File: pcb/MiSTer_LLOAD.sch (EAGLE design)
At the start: 22 parts, among them K1 692121030100

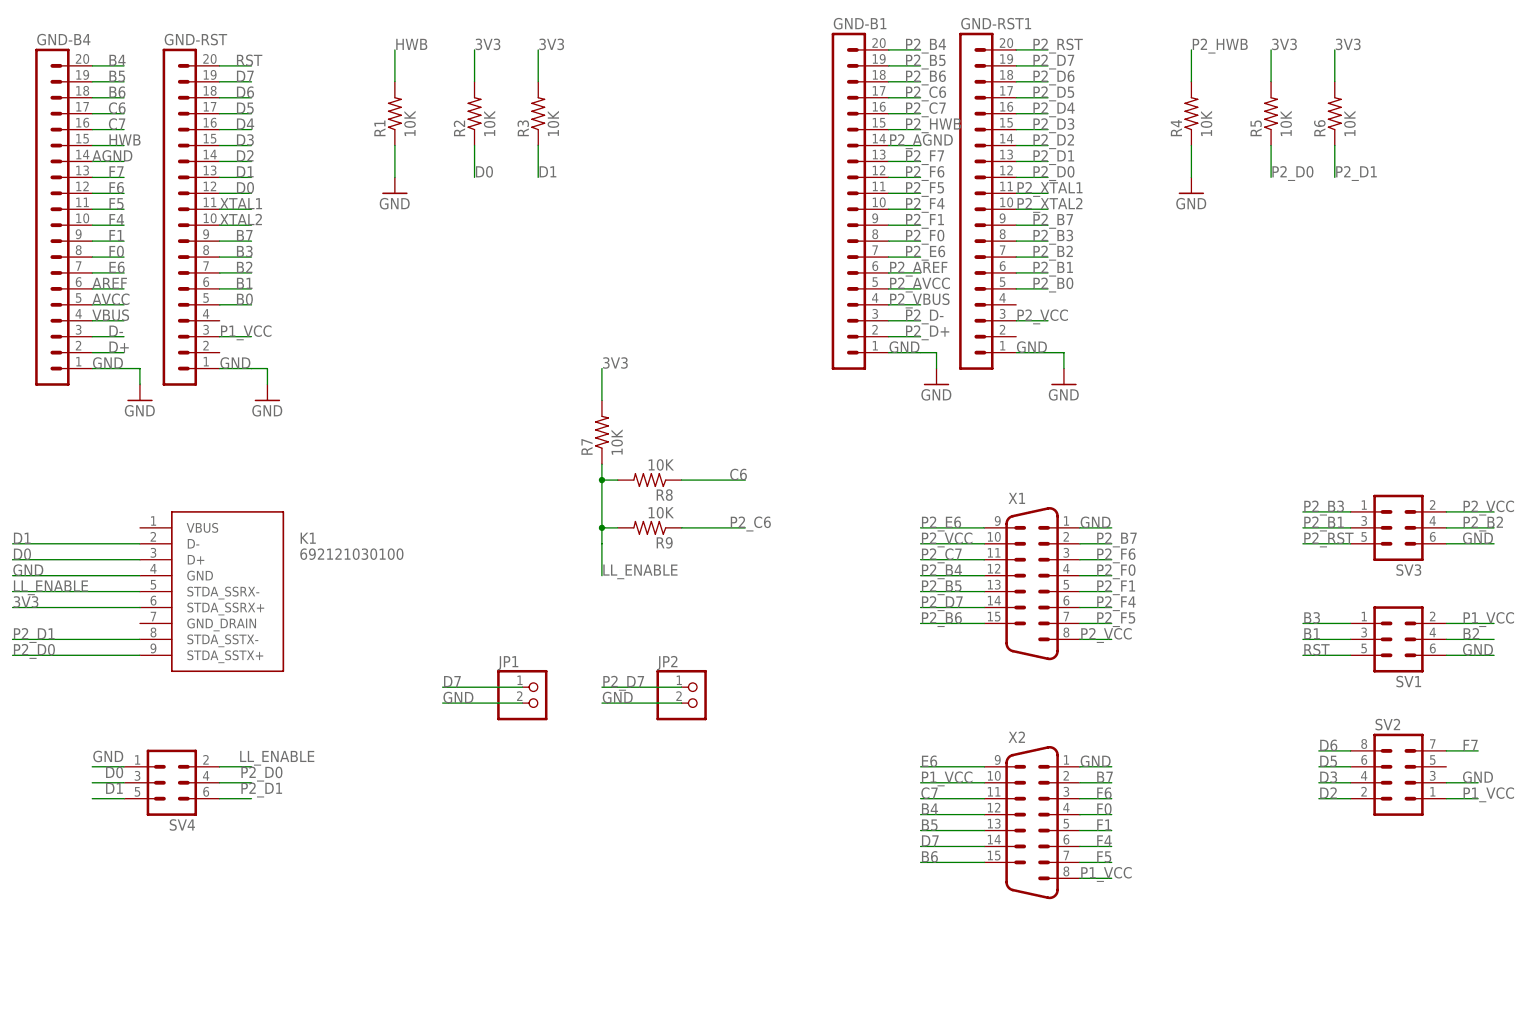
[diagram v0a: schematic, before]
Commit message: Proto v0.3 PCB - It does not rely on Serial IO VCC anymore
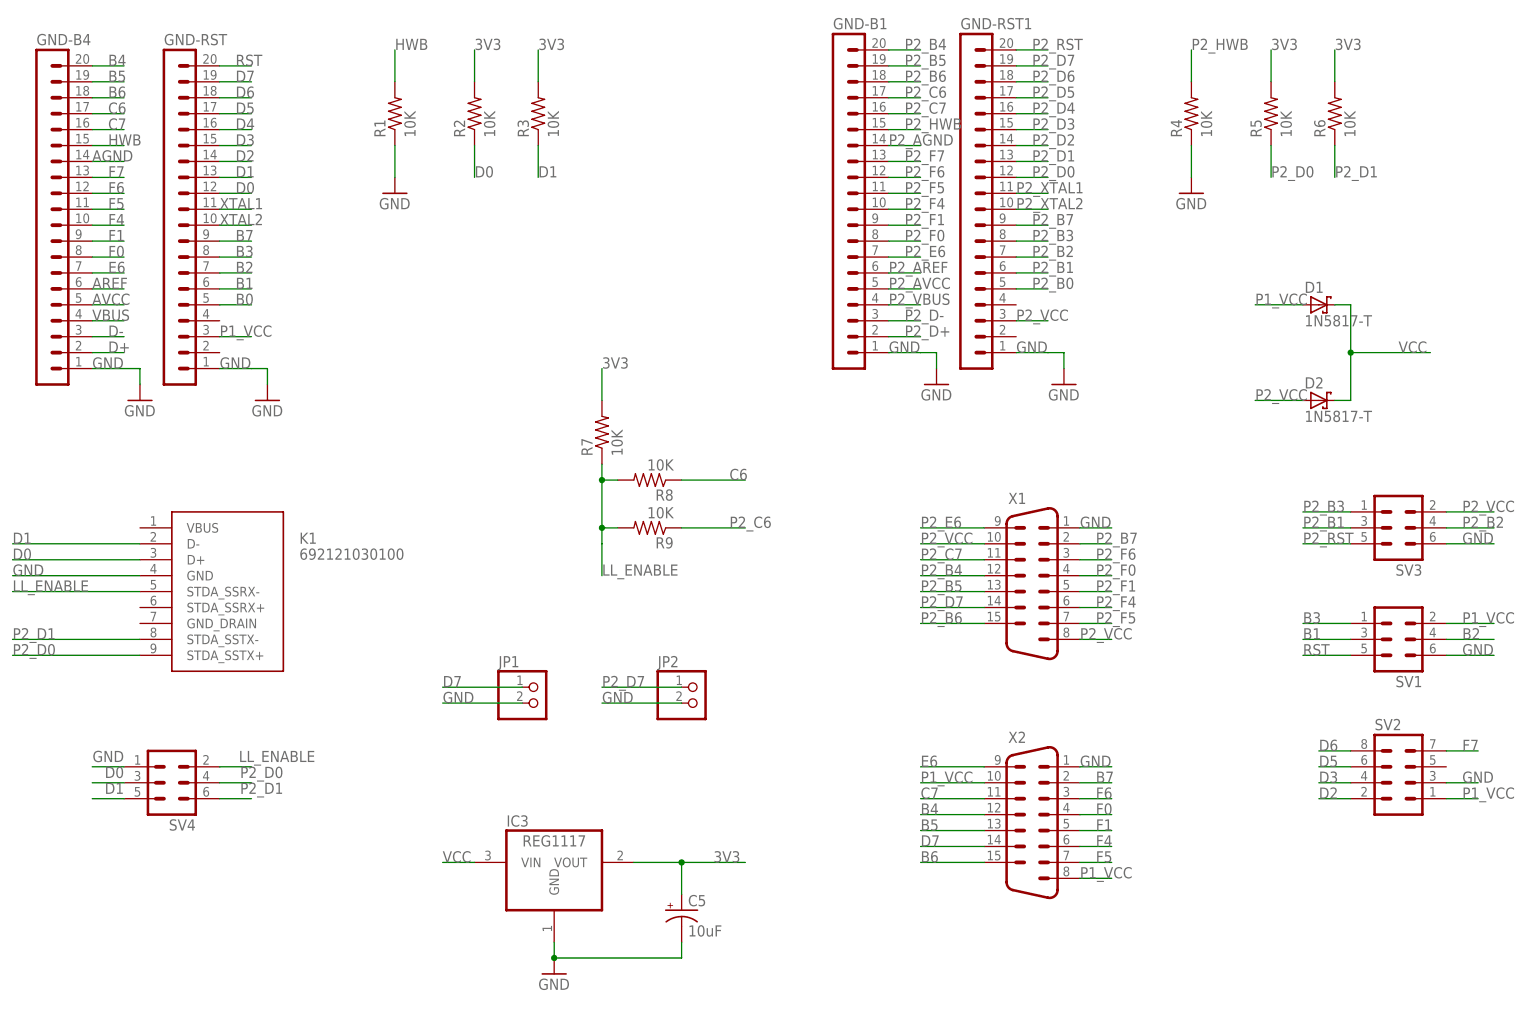
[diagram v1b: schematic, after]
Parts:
- added C5: 10uF, rcl:CPOL-USE2.5-6
- added D1, D2: 1N5817-T, diode:1N5817-T
- added IC3: REG1117, burr-brown:REG1117
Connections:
- new net VCC: D1.C, D2.C, IC3.VIN
- net 3V3: now also C5.+, IC3.VOUT; no longer K1.STDA_SSRX+
- net GND: now also C5.-, IC3.GND
- net P1_VCC: now also D1.A
- net P2_VCC: now also D2.A
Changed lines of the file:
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@@
 <part name="JP1" library="pinhead" deviceset="PINHD-1X2" device=""/>
 <part name="JP2" library="pinhead" deviceset="PINHD-1X2" device=""/>
+<part name="IC3" library="burr-brown" deviceset="REG1117" device=""/>
+<part name="GND7" library="supply1" deviceset="GND" device=""/>
+<part name="C5" library="rcl" deviceset="CPOL-US" device="E2.5-6" value="10uF"/>
+<part name="D1" library="diode" deviceset="1N581*" device="" technology="7-T"/>
+<part name="D2" library="diode" deviceset="1N581*" device="" technology="7-T"/>
 </parts>
 <sheets>
@@
 <instance part="JP1" gate="G$1" x="-35.56" y="-99.06"/>
 <instance part="JP2" gate="G$1" x="-10.16" y="-99.06"/>
+<instance part="IC3" gate="G$1" x="-33.02" y="-124.46"/>
+<instance part="GND7" gate="1" x="-33.02" y="-142.24"/>
+<instance part="C5" gate="G$1" x="-12.7" y="-132.08"/>
+<instance part="D1" gate="G$1" x="88.9" y="-35.56"/>
+<instance part="D2" gate="G$1" x="88.9" y="-50.8"/>
 </instances>
 <busses>
@@
 <label x="-25.4" y="-99.06" size="1.778" layer="95"/>
 </segment>
+<segment>
+<pinref part="IC3" gate="G$1" pin="GND"/>
+<pinref part="GND7" gate="1" pin="GND"/>
+<wire x1="-33.02" y1="-137.16" x2="-33.02" y2="-139.7" width="0.1524" layer="91"/>
+<pinref part="C5" gate="G$1" pin="-"/>
+<wire x1="-33.02" y1="-139.7" x2="-12.7" y2="-139.7" width="0.1524" layer="91"/>
+<wire x1="-12.7" y1="-139.7" x2="-12.7" y2="-137.16" width="0.1524" layer="91"/>
+<junction x="-33.02" y="-139.7"/>
+</segment>
 </net>
 <net name="RST" class="0">
@@
 <net name="3V3" class="0">
 <segment>
-<pinref part="K1" gate="G$1" pin="STDA_SSRX+"/>
-<wire x1="-99.06" y1="-83.82" x2="-119.38" y2="-83.82" width="0.1524" layer="91"/>
-<label x="-119.38" y="-83.82" size="1.778" layer="95"/>
-</segment>
-<segment>
 <pinref part="R2" gate="G$1" pin="2"/>
 <wire x1="-45.72" y1="0" x2="-45.72" y2="5.08" width="0.1524" layer="91"/>
@@
 <wire x1="-25.4" y1="-50.8" x2="-25.4" y2="-45.72" width="0.1524" layer="91"/>
 <label x="-25.4" y="-45.72" size="1.778" layer="95"/>
+</segment>
+<segment>
+<pinref part="IC3" gate="G$1" pin="VOUT"/>
+<wire x1="-20.32" y1="-124.46" x2="-12.7" y2="-124.46" width="0.1524" layer="91"/>
+<pinref part="C5" gate="G$1" pin="+"/>
+<wire x1="-12.7" y1="-124.46" x2="-2.54" y2="-124.46" width="0.1524" layer="91"/>
+<wire x1="-12.7" y1="-129.54" x2="-12.7" y2="-124.46" width="0.1524" layer="91"/>
+<junction x="-12.7" y="-124.46"/>
+<label x="-7.62" y="-124.46" size="1.778" layer="95"/>
 </segment>
 </net>
@@
 <pinref part="SV2" gate="G$1" pin="1"/>
 </segment>
+<segment>
+<wire x1="86.36" y1="-35.56" x2="78.74" y2="-35.56" width="0.1524" layer="91"/>
+<label x="78.74" y="-35.56" size="1.778" layer="95"/>
+<pinref part="D1" gate="G$1" pin="A"/>
+</segment>
 </net>
 <net name="P2_VCC" class="0">
@@
 <label x="111.76" y="-68.58" size="1.778" layer="95"/>
 </segment>
-</net>
+<segment>
+<wire x1="86.36" y1="-50.8" x2="78.74" y2="-50.8" width="0.1524" layer="91"/>
+<label x="78.74" y="-50.8" size="1.778" layer="95"/>
+<pinref part="D2" gate="G$1" pin="A"/>
+</segment>
+</net>
+<net name="VCC" class="0">
+<segment>
+<pinref part="IC3" gate="G$1" pin="VIN"/>
+<wire x1="-45.72" y1="-124.46" x2="-50.8" y2="-124.46" width="0.1524" layer="91"/>
+<label x="-50.8" y="-124.46" size="1.778" layer="95"/>
+</segment>
+<segment>
+<wire x1="93.98" y1="-43.18" x2="106.68" y2="-43.18" width="0.1524" layer="91"/>
+<wire x1="91.44" y1="-35.56" x2="93.98" y2="-35.56" width="0.1524" layer="91"/>
+<wire x1="93.98" y1="-35.56" x2="93.98" y2="-43.18" width="0.1524" layer="91"/>
+<wire x1="91.44" y1="-50.8" x2="93.98" y2="-50.8" width="0.1524" layer="91"/>
+<wire x1="93.98" y1="-50.8" x2="93.98" y2="-43.18" width="0.1524" layer="91"/>
+<junction x="93.98" y="-43.18"/>
+<label x="101.6" y="-43.18" size="1.778" layer="95"/>
+<pinref part="D1" gate="G$1" pin="C"/>
+<pinref part="D2" gate="G$1" pin="C"/>
+</segment>
+</net>

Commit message: Promoting LLOAD PCB to v1.0
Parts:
- removed SV2: (no value), con-lstb:MA04-2
- removed SV4: (no value), con-lstb:MA03-2
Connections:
- net 3V3: now also X1.10, X2.10
- net D0: no longer SV4.3
- net D1: no longer SV4.5
- net D2: no longer SV2.2
- net D3: no longer SV2.4
- net D5: no longer SV2.6
- net D6: no longer SV2.8
- net F7: no longer SV2.7
- net GND: no longer SV2.3, SV4.1
- net LL_ENABLE: no longer SV4.2
- net P1_VCC: no longer SV2.1, X2.10
- net P2_D0: no longer SV4.4
- net P2_D1: no longer SV4.6
- net P2_VCC: no longer X1.10
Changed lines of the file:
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@@
 <part name="FRAME1" library="frames" deviceset="A4L-LOC" device=""/>
 <part name="X2" library="con-subd" deviceset="M15" device="HP"/>
-<part name="SV2" library="con-lstb" deviceset="MA04-2" device=""/>
 <part name="R1" library="rcl" deviceset="R-US_" device="0207/10" value="10K"/>
 <part name="GND3" library="supply1" deviceset="GND" device=""/>
@@
 <part name="R8" library="rcl" deviceset="R-US_" device="0207/10" value="10K"/>
 <part name="R9" library="rcl" deviceset="R-US_" device="0207/10" value="10K"/>
-<part name="SV4" library="con-lstb" deviceset="MA03-2" device=""/>
 <part name="JP1" library="pinhead" deviceset="PINHD-1X2" device=""/>
 <part name="JP2" library="pinhead" deviceset="PINHD-1X2" device=""/>
@@
 <instance part="FRAME1" gate="G$1" x="-132.08" y="-162.56"/>
 <instance part="X2" gate="-1" x="43.18" y="-116.84"/>
-<instance part="SV2" gate="G$1" x="101.6" y="-109.22"/>
 <instance part="R1" gate="G$1" x="-58.42" y="-5.08" rot="R90"/>
 <instance part="GND3" gate="1" x="-58.42" y="-17.78"/>
@@
 <instance part="R8" gate="G$1" x="-17.78" y="-63.5" rot="R180"/>
 <instance part="R9" gate="G$1" x="-17.78" y="-71.12" rot="R180"/>
-<instance part="SV4" gate="1" x="-93.98" y="-111.76" rot="R180"/>
 <instance part="JP1" gate="G$1" x="-35.56" y="-99.06"/>
 <instance part="JP2" gate="G$1" x="-10.16" y="-99.06"/>
@@
 <pinref part="GND-B4" gate="1" pin="13"/>
 </segment>
-<segment>
-<wire x1="109.22" y1="-106.68" x2="114.3" y2="-106.68" width="0.1524" layer="91"/>
-<label x="111.76" y="-106.68" size="1.778" layer="95"/>
-<pinref part="SV2" gate="G$1" pin="7"/>
-</segment>
 </net>
 <net name="F6" class="0">
@@
 </segment>
 <segment>
-<wire x1="109.22" y1="-111.76" x2="114.3" y2="-111.76" width="0.1524" layer="91"/>
-<label x="111.76" y="-111.76" size="1.778" layer="95"/>
-<pinref part="SV2" gate="G$1" pin="3"/>
-</segment>
-<segment>
 <pinref part="R1" gate="G$1" pin="1"/>
 <pinref part="GND3" gate="1" pin="GND"/>
@@
 <wire x1="109.22" y1="-73.66" x2="116.84" y2="-73.66" width="0.1524" layer="91"/>
 <label x="111.76" y="-73.66" size="1.778" layer="95"/>
-</segment>
-<segment>
-<pinref part="SV4" gate="1" pin="1"/>
-<wire x1="-101.6" y1="-109.22" x2="-106.68" y2="-109.22" width="0.1524" layer="91"/>
-<label x="-101.6" y="-106.68" size="1.778" layer="95" rot="R180"/>
 </segment>
 <segment>
@@
 <pinref part="GND-RST" gate="1" pin="18"/>
 </segment>
-<segment>
-<wire x1="93.98" y1="-106.68" x2="88.9" y2="-106.68" width="0.1524" layer="91"/>
-<label x="88.9" y="-106.68" size="1.778" layer="95"/>
-<pinref part="SV2" gate="G$1" pin="8"/>
-</segment>
 </net>
 <net name="D5" class="0">
@@
 <pinref part="GND-RST" gate="1" pin="17"/>
 </segment>
-<segment>
-<wire x1="93.98" y1="-109.22" x2="88.9" y2="-109.22" width="0.1524" layer="91"/>
-<label x="88.9" y="-109.22" size="1.778" layer="95"/>
-<pinref part="SV2" gate="G$1" pin="6"/>
-</segment>
 </net>
 <net name="D4" class="0">
@@
 <pinref part="GND-RST" gate="1" pin="15"/>
 </segment>
-<segment>
-<wire x1="93.98" y1="-111.76" x2="88.9" y2="-111.76" width="0.1524" layer="91"/>
-<label x="88.9" y="-111.76" size="1.778" layer="95"/>
-<pinref part="SV2" gate="G$1" pin="4"/>
-</segment>
 </net>
 <net name="D2" class="0">
@@
 <pinref part="GND-RST" gate="1" pin="14"/>
 </segment>
-<segment>
-<wire x1="93.98" y1="-114.3" x2="88.9" y2="-114.3" width="0.1524" layer="91"/>
-<label x="88.9" y="-114.3" size="1.778" layer="95"/>
-<pinref part="SV2" gate="G$1" pin="2"/>
-</segment>
 </net>
 <net name="D1" class="0">
@@
 <label x="-35.56" y="-15.24" size="1.778" layer="95"/>
 </segment>
-<segment>
-<pinref part="SV4" gate="1" pin="5"/>
-<wire x1="-101.6" y1="-114.3" x2="-106.68" y2="-114.3" width="0.1524" layer="91"/>
-<label x="-101.6" y="-111.76" size="1.778" layer="95" rot="R180"/>
-</segment>
 </net>
 <net name="D0" class="0">
@@
 <label x="-45.72" y="-15.24" size="1.778" layer="95"/>
 </segment>
-<segment>
-<pinref part="SV4" gate="1" pin="3"/>
-<wire x1="-101.6" y1="-111.76" x2="-106.68" y2="-111.76" width="0.1524" layer="91"/>
-<label x="-101.6" y="-109.22" size="1.778" layer="95" rot="R180"/>
-</segment>
 </net>
 <net name="XTAL1" class="0">
@@
 <label x="91.44" y="-15.24" size="1.778" layer="95"/>
 </segment>
-<segment>
-<pinref part="SV4" gate="1" pin="6"/>
-<wire x1="-86.36" y1="-114.3" x2="-81.28" y2="-114.3" width="0.1524" layer="91"/>
-<label x="-76.2" y="-111.76" size="1.778" layer="95" rot="R180"/>
-</segment>
 </net>
 <net name="P2_D0" class="0">
@@
 <wire x1="81.28" y1="-10.16" x2="81.28" y2="-15.24" width="0.1524" layer="91"/>
 <label x="81.28" y="-15.24" size="1.778" layer="95"/>
-</segment>
-<segment>
-<pinref part="SV4" gate="1" pin="4"/>
-<wire x1="-86.36" y1="-111.76" x2="-81.28" y2="-111.76" width="0.1524" layer="91"/>
-<label x="-76.2" y="-109.22" size="1.778" layer="95" rot="R180"/>
 </segment>
 </net>
@@
 <junction x="-12.7" y="-124.46"/>
 <label x="-7.62" y="-124.46" size="1.778" layer="95"/>
+</segment>
+<segment>
+<wire x1="35.56" y1="-73.66" x2="25.4" y2="-73.66" width="0.1524" layer="91"/>
+<label x="25.4" y="-73.66" size="1.778" layer="95"/>
+<pinref part="X1" gate="-1" pin="10"/>
+</segment>
+<segment>
+<wire x1="35.56" y1="-111.76" x2="25.4" y2="-111.76" width="0.1524" layer="91"/>
+<label x="25.4" y="-111.76" size="1.778" layer="95"/>
+<pinref part="X2" gate="-1" pin="10"/>
 </segment>
 </net>
@@
 <wire x1="-25.4" y1="-73.66" x2="-25.4" y2="-78.74" width="0.1524" layer="91"/>
 </segment>
-<segment>
-<pinref part="SV4" gate="1" pin="2"/>
-<wire x1="-86.36" y1="-109.22" x2="-81.28" y2="-109.22" width="0.1524" layer="91"/>
-<label x="-71.12" y="-106.68" size="1.778" layer="95" rot="R180"/>
-</segment>
 </net>
 <net name="P1_VCC" class="0">
@@
 </segment>
 <segment>
-<wire x1="35.56" y1="-111.76" x2="25.4" y2="-111.76" width="0.1524" layer="91"/>
-<label x="25.4" y="-111.76" size="1.778" layer="95"/>
-<pinref part="X2" gate="-1" pin="10"/>
-</segment>
-<segment>
 <wire x1="50.8" y1="-127" x2="55.88" y2="-127" width="0.1524" layer="91"/>
 <label x="50.8" y="-127" size="1.778" layer="95"/>
@@
 </segment>
 <segment>
-<wire x1="109.22" y1="-114.3" x2="114.3" y2="-114.3" width="0.1524" layer="91"/>
-<label x="111.76" y="-114.3" size="1.778" layer="95"/>
-<pinref part="SV2" gate="G$1" pin="1"/>
-</segment>
-<segment>
 <wire x1="86.36" y1="-35.56" x2="78.74" y2="-35.56" width="0.1524" layer="91"/>
 <label x="78.74" y="-35.56" size="1.778" layer="95"/>
@@
 </segment>
 <segment>
-<wire x1="35.56" y1="-73.66" x2="25.4" y2="-73.66" width="0.1524" layer="91"/>
-<label x="25.4" y="-73.66" size="1.778" layer="95"/>
-<pinref part="X1" gate="-1" pin="10"/>
-</segment>
-<segment>

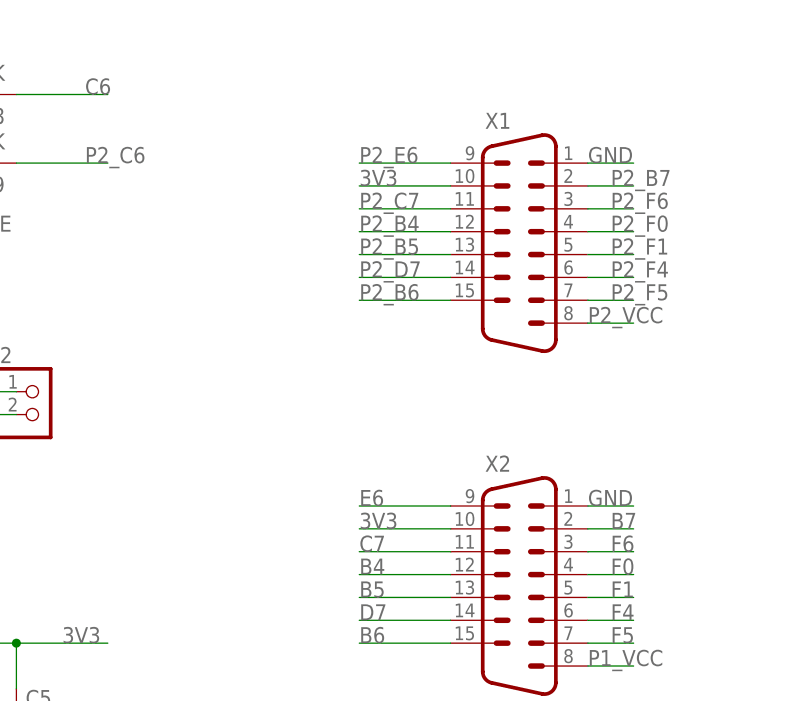
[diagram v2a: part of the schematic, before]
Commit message: Removed alternate VCC (3.3v) from DB15 pin 10. This will not make it directly compatible with supergun input, but at least no harm will be done in case someone inadvertently uses a supergun with it. Neo Geo and Neo Geo CD are still welcome in both revisions.
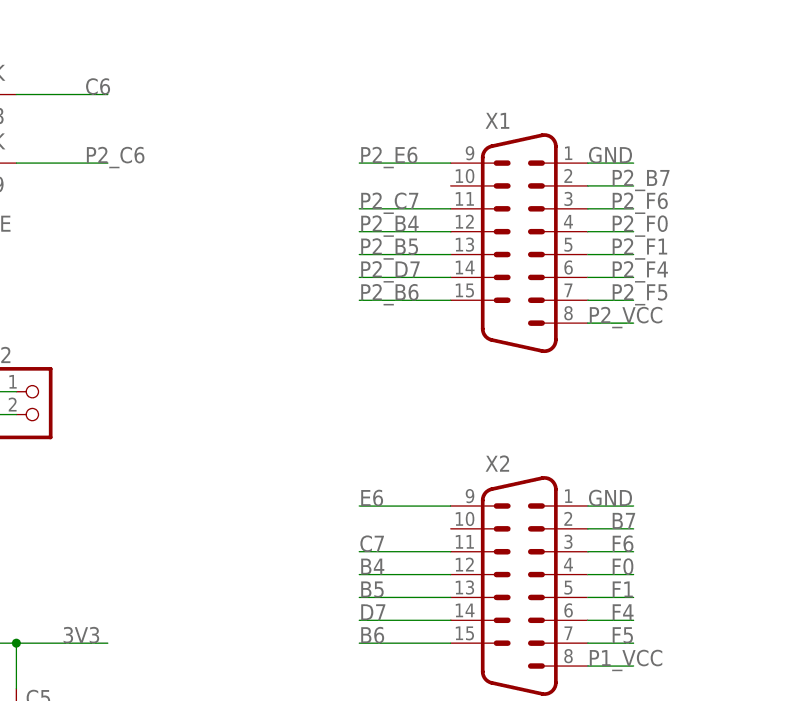
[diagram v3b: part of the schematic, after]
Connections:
- net 3V3: no longer X1.10, X2.10
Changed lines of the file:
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@@
 <label x="-7.62" y="-124.46" size="1.778" layer="95"/>
-</segment>
-<segment>
-<wire x1="35.56" y1="-73.66" x2="25.4" y2="-73.66" width="0.1524" layer="91"/>
-<label x="25.4" y="-73.66" size="1.778" layer="95"/>
-<pinref part="X1" gate="-1" pin="10"/>
-</segment>
-<segment>
-<wire x1="35.56" y1="-111.76" x2="25.4" y2="-111.76" width="0.1524" layer="91"/>
-<label x="25.4" y="-111.76" size="1.778" layer="95"/>
-<pinref part="X2" gate="-1" pin="10"/>
 </segment>
 </net>
